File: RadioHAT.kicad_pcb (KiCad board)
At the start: 2 copper layers, 65 x 56.5 mm, 36 parts, among them J1 RPi_GPIO, J3 Conn_02x06_Odd_Even, J4 Conn_02x07_Odd_Even, U1 INA219AxD, U2 LP3855-ADJ

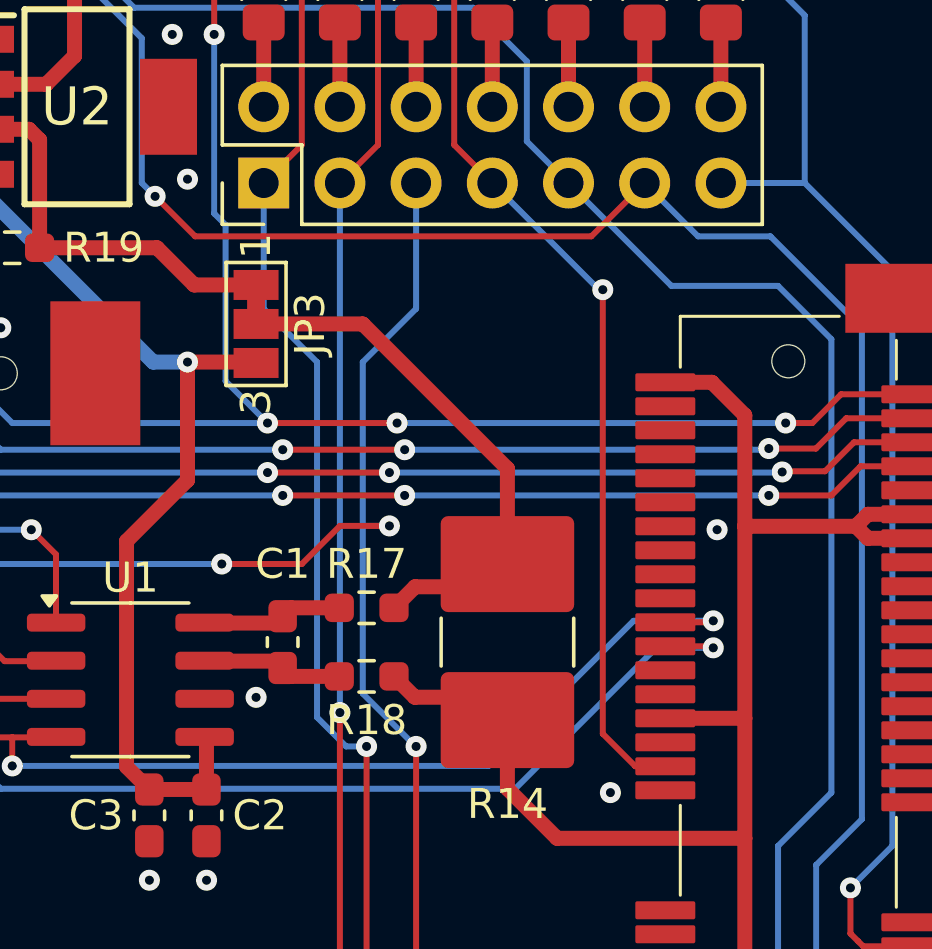
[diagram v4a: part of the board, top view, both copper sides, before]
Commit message: Update to use new RPi HAT
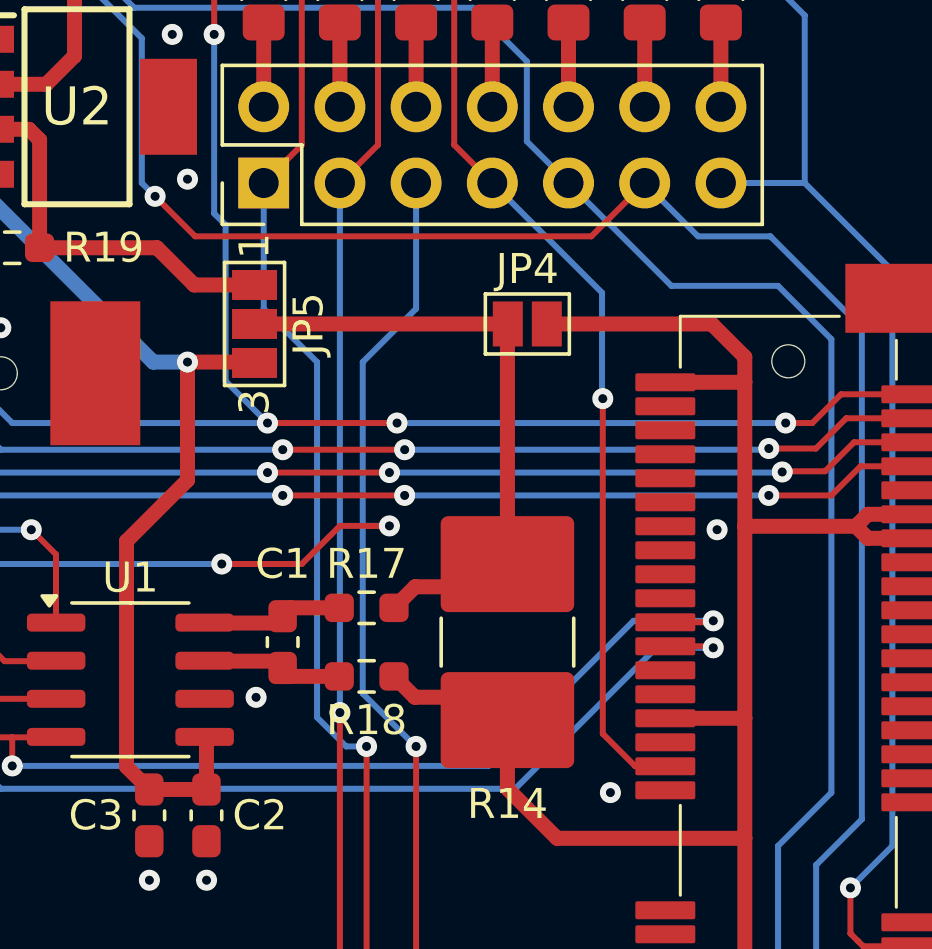
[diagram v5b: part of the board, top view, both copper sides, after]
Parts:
- removed JP3: SolderJumper_3_Bridged12, Jumper:SolderJumper-3_P1.3mm_Bridged12_Pad1.0x1.5mm_NumberLabels
- added JP4: SolderJumper_2_Open, Jumper:SolderJumper-2_P1.3mm_Open_Pad1.0x1.5mm, F.Cu at (157.6, 91.4)
- added JP5: SolderJumper_3_Open, Jumper:SolderJumper-3_P1.3mm_Open_Pad1.0x1.5mm_NumberLabels, F.Cu at (148.5, 91.4)
- J1: footprint rpi-hat:RPI_Hat_B+ -> RadioHAT:RPI_Hat_B+
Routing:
- net +3.3V_PCI: track 52.8 -> 61.4 mm
- net Net-(JP4-B): track 17.9 -> 20.8 mm
